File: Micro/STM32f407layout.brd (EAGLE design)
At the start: 100 x 80 mm, 41 parts, among them Q1 ASF, U1 LM1085IS-3.3

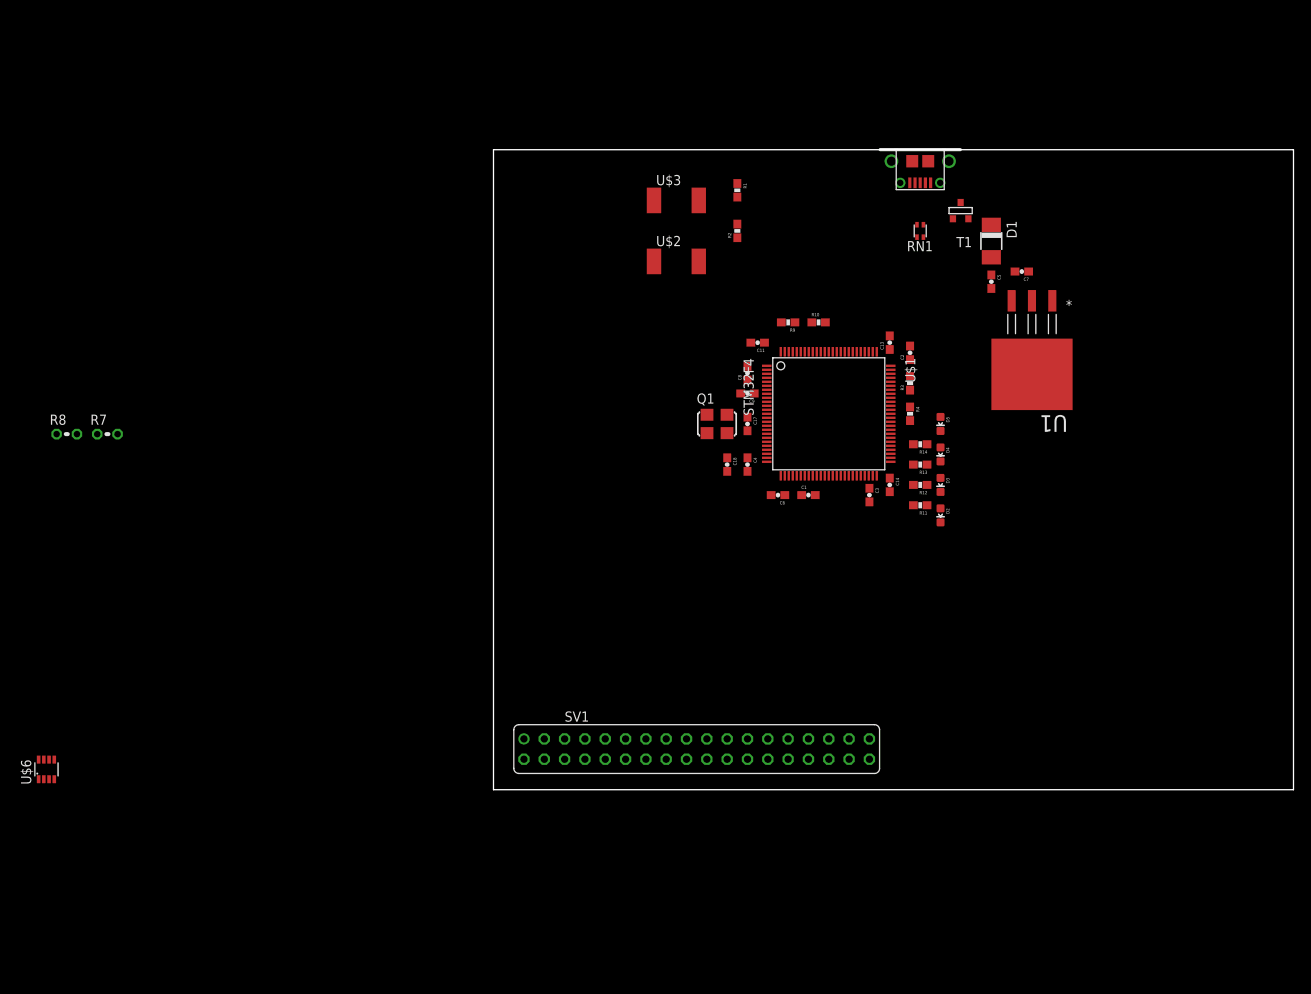
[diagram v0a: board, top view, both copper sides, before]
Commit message: worked on board layout, set initial width requirements
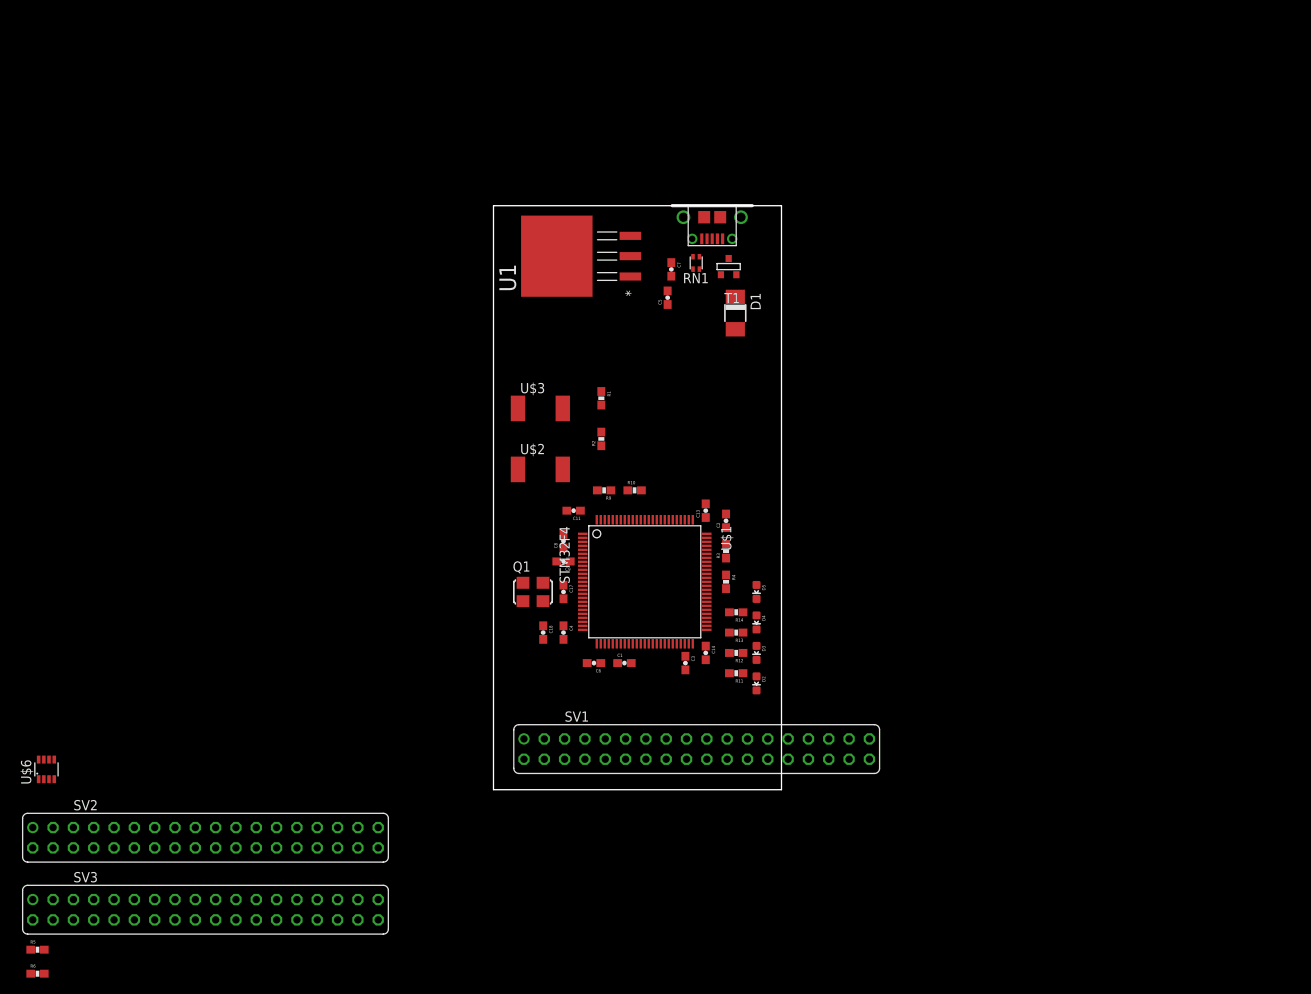
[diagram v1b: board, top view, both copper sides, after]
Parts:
- removed R7: 120, resistor:0204V
- removed R8: 100k, resistor:0204V
- added R5: 120, SparkFun-Passives:0603-RES
- added R6: 100K, SparkFun-Passives:0603-RES
- added SV2, SV3: (no value), Connectors:FE18-2
- moved U1 61.0 mm to (8.07, 66.7), turned to 90 degrees
- moved C7 43.8 mm to (22.2, 65.0), turned to 270 degrees
- moved C5 40.5 mm to (21.8, 61.5), turned to 90 degrees
- moved D1 33.2 mm to (30.2, 59.6)
- moved C11 31.1 mm to (10.0, 34.9)
- moved C3 31.1 mm to (24.0, 15.8)
- moved R11 31.1 mm to (30.3, 14.6)
- moved R12 31.1 mm to (30.3, 17.1)
- moved R13 31.1 mm to (30.3, 19.6)
- moved R14 31.1 mm to (30.3, 22.2)
- moved R4 31.1 mm to (29.1, 26.0)
- moved C1 31.1 mm to (16.4, 15.8)
- moved C13 31.1 mm to (26.5, 34.9)
- moved C14 31.1 mm to (26.5, 17.1)
- moved C17 31.1 mm to (8.75, 24.7)
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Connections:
- removed net N$13: R8.1, U$6.8
- new net N$11: R6.2, U$6.8
- net CANH1: now also R5.2; no longer R7.1
- net CANL1: now also R5.1; no longer R7.2
- net GND: now also R6.1; no longer R8.2
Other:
- board size 100 x 80 mm -> 36 x 73 mm

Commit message: Updated Board
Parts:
- removed SV1, SV2, SV3: (no value), Connectors:FE18-2
- added R7: 4.7K, SparkFun-Passives:0603-RES
- moved R6 94.5 mm to (30.0, 14.0), turned to 270 degrees
- moved R5 92.0 mm to (30.0, 10.0), turned to 90 degrees
- moved U$6 82.7 mm to (26.5, 9.88), turned to 270 degrees
- moved U$4 69.3 mm to (-0.01, 9.34), turned to 270 degrees
- moved RN1 59.4 mm to (7.15, 9.34), turned to 270 degrees
- moved T1 57.3 mm to (7.61, 12.4), turned to 270 degrees
- moved D1 50.3 mm to (5.58, 15.8), turned to 180 degrees
- moved D2 34.2 mm to (15.7, 42.9), turned to 270 degrees
- moved D5 33.9 mm to (4.28, 42.9), turned to 270 degrees
- moved D3 33.2 mm to (11.9, 42.9), turned to 270 degrees
- moved D4 33.1 mm to (8.09, 42.9), turned to 270 degrees
- moved R11 30.3 mm to (14.4, 40.3), turned to 270 degrees
- moved R14 29.7 mm to (6.82, 40.3), turned to 270 degrees
- moved R12 29.7 mm to (11.9, 40.3), turned to 270 degrees
- moved R13 29.5 mm to (9.36, 40.3), turned to 270 degrees
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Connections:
- removed net CAN1_RX: SV1.1
- removed net CAN1_TX: SV1.3
- new net TEMP_SENSE_INFO: R7.1, U$1.P81
- net +3V3: now also R7.2; no longer SV1.4
- net +5V: no longer SV1.2
- net CAN2_RX: no longer SV1.5
- net CAN2_TX: no longer SV1.7
- net GND: no longer SV1.12, SV1.6, SV1.8
- net I2C1_SCL: no longer SV1.33
- net I2C1_SDA: no longer SV1.35
- net I2C3_SCL: no longer SV1.17
- net I2C3_SDA: no longer SV1.19
- net OSC_IN: no longer SV1.15
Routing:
- net +3V3: track 0.00 -> 84.9 mm, vias 0 -> 5
- net N$9: track 0.00 -> 33.4 mm
- net N$16: track 0.00 -> 32.0 mm
- net N$8: track 0.00 -> 30.6 mm
- net N$19: track 0.00 -> 28.7 mm
- net N$22: track 0.00 -> 6.27 mm, vias 0 -> 1
- net N$15: track 0.00 -> 4.12 mm
- net OSC_IN: track 0.00 -> 3.49 mm
- net N$11: track 0.00 -> 3.46 mm
- net N$10: track 0.00 -> 3.18 mm
- net N$17: track 0.00 -> 2.85 mm
- net N$5: track 0.00 -> 2.83 mm
- net CANH1: track 0.00 -> 2.50 mm
- net CANL1: track 0.00 -> 2.40 mm
- net N$6: track 0.00 -> 2.40 mm
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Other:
- board size 36 x 73 mm -> 36 x 76 mm

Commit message: More Board Updates
Remind myself to switch LED pins
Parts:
- removed R7: 4.7K, SparkFun-Passives:0603-RES
- moved U$3 52.2 mm to (29.9, 8.66)
- moved R1 45.9 mm to (32.9, 13.5), flipped to the bottom, turned to 0 degrees
- moved R9 27.7 mm to (29.6, 22.8), turned to 45 degrees
- moved R10 23.6 mm to (27.6, 16.0), turned to 225 degrees
- moved U$2 20.0 mm to (28.1, 41.0), turned to 180 degrees
- moved D5 18.9 mm to (1.12, 24.3), turned to 0 degrees
- moved R14 16.8 mm to (3.66, 23.8), turned to 45 degrees
- moved D4 16.4 mm to (1.12, 28.1), turned to 0 degrees
- moved D2 16.3 mm to (1.12, 35.7), turned to 0 degrees
- moved R2 15.4 mm to (23.4, 36.2), turned to 135 degrees
- moved D3 15.4 mm to (1.12, 31.9), turned to 0 degrees
- moved R13 13.3 mm to (3.66, 28.4), turned to 45 degrees
- moved R4 12.6 mm to (9.93, 20.0), turned to 135 degrees
- moved R11 11.8 mm to (3.56, 35.7), turned to 45 degrees
- moved R12 11.8 mm to (3.66, 31.9), turned to 45 degrees
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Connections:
- removed net CAN2_RX: U$1.P91
- removed net CAN2_TX: U$1.P92
- removed net TEMP_SENSE_INFO: R7.1, U$1.P81
- net +3V3: no longer R7.2
- net CAN_RX: now also U$1.P91
- net CAN_TX: now also U$1.P92
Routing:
- net N$9: track 33.4 -> 0.00 mm
- net N$16: track 32.0 -> 0.00 mm
- net N$8: track 30.6 -> 0.00 mm
- net N$19: track 28.7 -> 0.00 mm
- net I2C1_SCL: track 0.00 -> 25.7 mm
- net I2C1_SDA: track 0.00 -> 23.9 mm
- net I2C3_SCL: track 0.00 -> 23.0 mm, vias 0 -> 1
- net I2C3_SDA: track 0.00 -> 21.6 mm, vias 0 -> 1
- net N$3: track 0.00 -> 19.1 mm, vias 0 -> 1
- net USB_D+: track 0.00 -> 12.1 mm
- net USB_D-: track 0.00 -> 11.5 mm
- net N$4: track 0.00 -> 10.5 mm
- net CAN_TX: track 0.00 -> 7.36 mm
- net CAN_RX: track 0.00 -> 5.52 mm
- net N$15: track 4.12 -> 0.00 mm
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
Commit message: Made changes to the micro board
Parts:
- removed C5, C7: 0.22uF, SparkFun-Passives:0603-CAP
- removed D1: (no value), DiscreteComponents:DO-214AC
- removed RN1: (no value), DiscreteComponents:EXBV4V
- removed T1: (no value), DiscreteComponents:SOT-23
- removed U$4: MICROUSB, Other:MICRO_B
- removed U1: LM1085IS-3.3, PowerComponents:TO254P1435X457-3N
- added C10, C12: 0.22uF, rcl:C0603
- added D6: (no value), DiscreteComponents:DO-214AC
- added RN2: (no value), DiscreteComponents:EXBV4V
- added SV1, SV2, SV3: (no value), con-lsta:FE08-2
- added SV4: (no value), con-lsta:FE07-2
- added T3: FDN340P, DiscreteComponents:SOT-23
- added T4: AP1117_LIN_REG, PowerComponents:SOT223
- added U$5: MICROUSB, Other:MICRO_B
- moved C1 57.5 mm to (68.0, 47.6), flipped to the top, turned to 0 degrees
- moved R4 56.7 mm to (34.6, 71.1), flipped to the bottom, turned to 0 degrees
- moved C8 53.7 mm to (55.8, 54.6), turned to 90 degrees
- moved R3 53.5 mm to (34.6, 64.9), flipped to the bottom, turned to 0 degrees
- moved R14 48.8 mm to (26.2, 67.2), turned to 0 degrees
- moved D5 48.0 mm to (22.6, 67.2), turned to 90 degrees
- moved R13 46.6 mm to (26.2, 69.1), turned to 0 degrees
- moved D4 46.3 mm to (22.6, 69.1), turned to 90 degrees
- moved R12 45.2 mm to (26.2, 71.1), turned to 0 degrees
- moved D3 44.7 mm to (22.6, 71.1), turned to 90 degrees
- moved C11 44.2 mm to (57.3, 47.5), turned to 180 degrees
- moved R11 43.7 mm to (26.2, 73.1), turned to 0 degrees
- moved Q1 43.5 mm to (68.1, 51.2), turned to 90 degrees
- moved D2 43.1 mm to (22.6, 73.1), turned to 90 degrees
- moved U$3 43.0 mm to (24.0, 51.3), turned to 270 degrees
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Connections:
- removed net ETC_MDC: U$1.P16
- removed net ETH_CRS_DV: U$1.P32
- removed net ETH_MDIO: U$1.P25
- removed net ETH_REF_CLK: U$1.P24
- removed net ETH_RXD0: U$1.P33
- removed net ETH_RXD1: U$1.P34
- removed net ETH_TXD0: U$1.P51
- removed net ETH_TXD1: U$1.P52
- removed net ETH_TX_EN: U$1.P48
- removed net N$10: T1.1, U$4.P1
- removed net N$16: R13.2, U$1.P60
- removed net N$19: R11.2, U$1.P58
- removed net N$22: C17.2, C18.2, U$1.P20
- removed net N$5: D1.C, T1.2
- removed net N$6: RN1.2, U$4.P3
- removed net N$7: RN1.1, U$4.P2
- removed net N$8: R12.2, U$1.P59
- removed net N$9: R14.2, U$1.P61
- removed net VCC: U$6.3
- new net CRS_DV: SV4.7, U$1.P32
- new net MDC: SV4.5, U$1.P16
- new net MDIO: SV4.6, U$1.P25
- new net N$12: RN2.1, U$5.P2
- new net N$24: RN2.2, U$5.P3
- new net N$57: T3.1, U$5.P1
- new net N$58: C12.1, D6.C, T3.2, T4.VIN
- new net PA10: SV2.14, U$1.P69
- new net PA13: U$1.P72
- new net PA14: U$1.P76
- new net PA15: U$1.P77
- new net PA5: U$1.P31
- new net PA9: SV2.13, U$1.P68
- new net PB0: U$1.P35
- new net PB1: U$1.P36
- new net PB10: U$1.P47
- new net PB14: U$1.P53
- new net PB15: U$1.P54
- new net PB2: U$1.P37
- new net PB3: U$1.P89
- new net PB4: SV1.11, U$1.P90
- new net PB9: SV1.16, U$1.P96
- new net PC0: SV3.1, U$1.P15
- new net PC10: SV1.1, U$1.P78
- new net PC11: SV1.2, U$1.P79
- new net PC12: SV1.3, U$1.P80
- new net PC13: SV3.6, U$1.P7
- new net PC14: SV3.5, U$1.P8
- new net PC15: SV3.4, U$1.P9
- new net PC2: U$1.P17
- new net PC3: U$1.P18
- new net PC6: SV2.8, U$1.P63
- new net PC7: SV2.9, U$1.P64
- new net PC8: SV2.10, U$1.P65
- new net PD0: SV1.4, U$1.P81
- new net PD1: SV1.5, U$1.P82
- new net PD10: U$1.P57
- new net PD11: R11.2, SV2.3, U$1.P58
- new net PD12: R12.2, SV2.4, U$1.P59
- new net PD13: R13.2, SV2.5, U$1.P60
- new net PD14: R14.2, SV2.6, U$1.P61
- new net PD15: SV2.7, U$1.P62
- new net PD2: SV1.6, U$1.P83
- new net PD3: SV1.7, U$1.P84
- new net PD4: SV1.8, U$1.P85
- new net PD5: SV1.9, U$1.P86
- new net PD6: SV1.10, U$1.P87
- new net PD7: U$1.P88
- new net PD8: SV2.1, U$1.P55
- new net PD9: SV2.2, U$1.P56
- new net PE0: U$1.P97
- new net PE1: U$1.P98
- new net PE10: U$1.P41
- new net PE11: U$1.P42
- new net PE12: U$1.P43
- new net PE13: U$1.P44
- new net PE14: U$1.P45
- new net PE15: U$1.P46
- new net PE2: SV3.16, U$1.P1
- new net PE3: SV3.15, U$1.P2
- new net PE4: SV3.14, U$1.P3
- new net PE5: SV3.13, U$1.P4
- new net PE6: SV3.12, U$1.P5
- new net PE7: U$1.P38
- new net PE8: U$1.P39
- new net PE9: U$1.P40
- new net PH1: SV3.2, U$1.P13
- new net REFCLK: SV4.8, U$1.P24
- new net RXD0: SV4.10, U$1.P33
- new net RXD1: SV4.9, U$1.P34
- new net TXD0: SV4.11, U$1.P51
- new net TXD1: SV4.14, U$1.P52
- new net TXEN: SV4.12, U$1.P48
- net +3V3: now also C10.1, SV2.16, SV3.10, SV3.8, SV4.1, SV4.2, T4.TAB, T4.VOUT, U$6.3; no longer C7.1, U1.2, U1.4
- net +5V: now also D6.A, T3.3; no longer C5.1, D1.A, T1.3, U1.3
- net CAN_RX: now also SV1.12
- net CAN_TX: now also SV1.13
- net GND: now also C10.2, C12.2, C17.2, C18.2, SV2.15, SV3.11, SV3.7, SV3.9, SV4.3, SV4.4, T4.GND, U$1.P20, U$5.GND1, U$5.GND2, U$5.GND3, U$5.GND4, U$5.GND7, U$5.GND8, U$5.P4, U$5.P5; no longer C5.2, C7.2, U$4.GND1, U$4.GND2, U$4.GND3, U$4.GND4, U$4.GND7, U$4.GND8, U$4.P4, U$4.P5, U1.1
- net I2C1_SCL: now also SV1.15
- net I2C1_SDA: now also SV1.14
- net I2C3_SCL: now also SV2.12
- net I2C3_SDA: now also SV2.11
- net OSC_IN: now also SV3.3
- net USB_D+: now also RN2.3; no longer RN1.3
- net USB_D-: now also RN2.4; no longer RN1.4
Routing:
- net +3V3: track 85.9 -> 145.8 mm, vias 8 -> 7
- net N$4: track 10.5 -> 47.6 mm, vias 0 -> 3
- net PD11: track 0.00 -> 35.0 mm, vias 0 -> 1
- net PD12: track 0.00 -> 33.9 mm, vias 0 -> 1
- net PD13: track 0.00 -> 32.5 mm, vias 0 -> 1
- net PD14: track 0.00 -> 31.0 mm, vias 0 -> 1
- net N$3: track 19.1 -> 35.6 mm, vias 1 -> 2
- net I2C3_SDA: track 21.6 -> 5.44 mm, vias 1 -> 0
- net PC0: track 0.00 -> 15.8 mm
- net GND: track 0.00 -> 15.3 mm, vias 0 -> 1
- net I2C1_SCL: track 25.7 -> 10.6 mm
- net N$57: track 0.00 -> 15.0 mm
- net OSC_IN: track 3.68 -> 18.4 mm
- net PC14: track 0.00 -> 14.4 mm
- net I2C3_SCL: track 23.0 -> 9.46 mm, vias 1 -> 0
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- added copper zone on layer 1, net +3V3
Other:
- board size 36 x 76 mm -> 100 x 80 mm

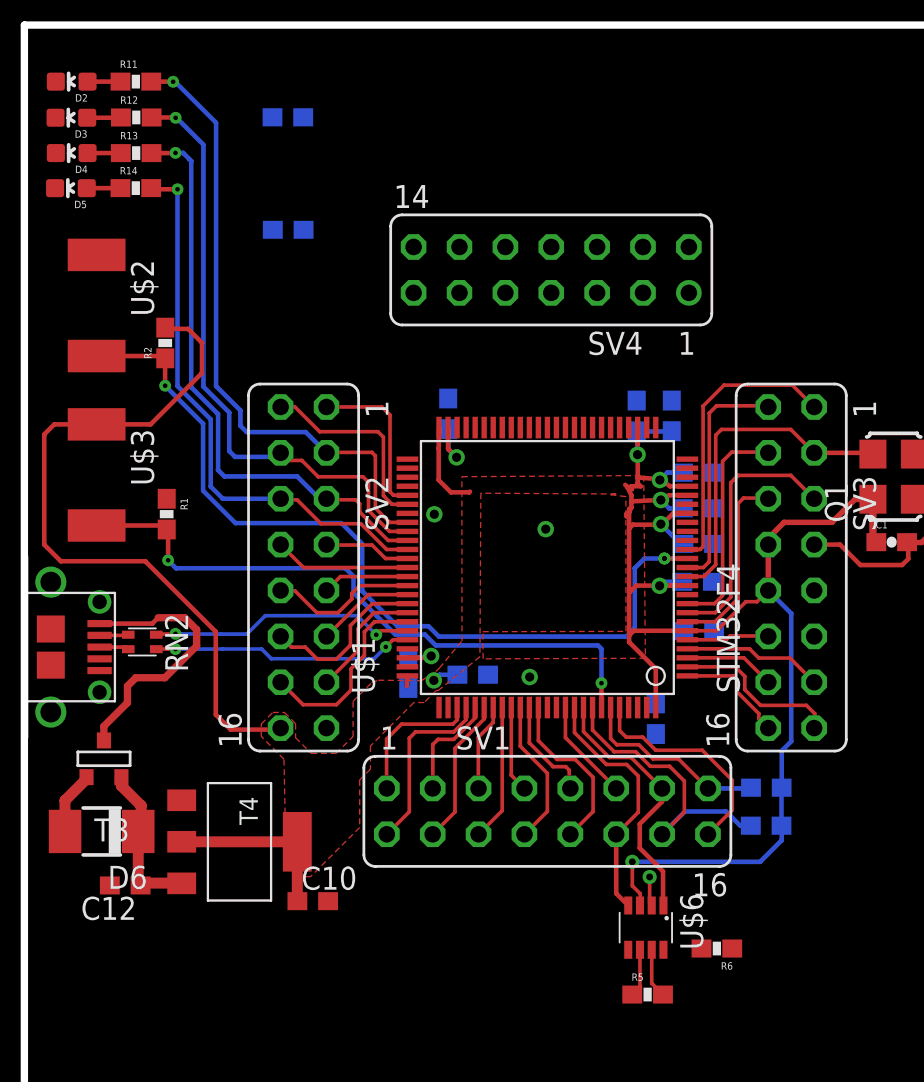
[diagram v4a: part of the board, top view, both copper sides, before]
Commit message: Updated Board on flight
moved TXD0 pin connection to not cross transmission lines
remove PC0 so can run MDC out. If it is a clock its pretty important
that it does not go under micro
may want to move xtal, bit far away probably wont be a problem but hf
signals do not like distance and things inbetween them
check via usage, use different ones , may want to stick to 1 size
move i2c resistors to bottom, connected them to 3v3
are linear regs noisey or is that switching? pretty sure it is switching
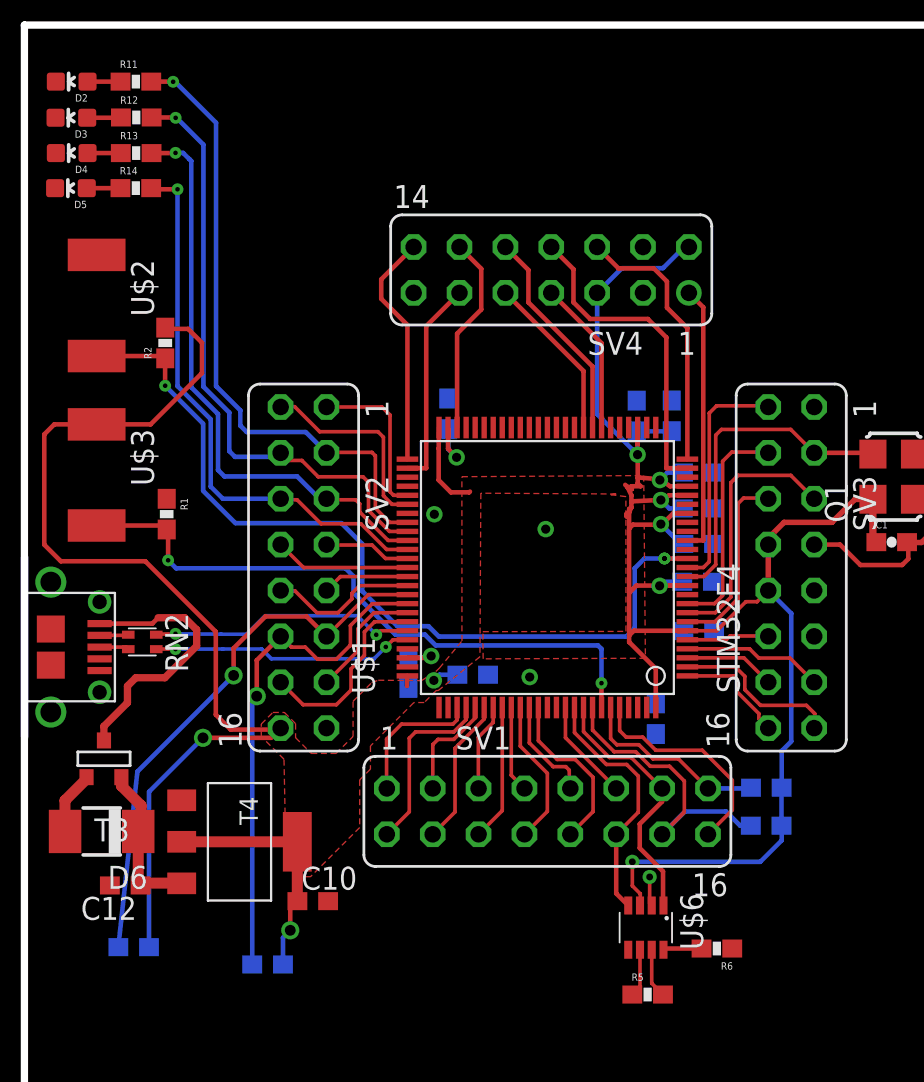
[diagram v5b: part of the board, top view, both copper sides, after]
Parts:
- moved R4 46.7 mm to (26.0, 25.1), turned to 180 degrees
- moved R3 40.7 mm to (33.5, 24.2), turned to 180 degrees
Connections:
- net +3V3: now also SV4.5; no longer SV4.1
- net MDC: now also SV4.1; no longer SV4.5
- net TXD0: now also SV4.14; no longer SV4.11
- net TXD1: now also SV4.11; no longer SV4.14
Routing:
- net +3V3: track 145.8 -> 184.5 mm, vias 7 -> 9
- net I2C3_SDA: track 5.44 -> 30.6 mm, vias 0 -> 1
- net I2C3_SCL: track 9.46 -> 28.3 mm, vias 0 -> 1
- net REFCLK: track 0.00 -> 17.9 mm
- net PC0: track 15.8 -> 0.00 mm
- net MDIO: track 0.00 -> 15.0 mm
- net MDC: track 0.00 -> 14.9 mm
- net TXD0: track 0.00 -> 13.1 mm
- net RXD0: track 0.00 -> 12.0 mm
- net TXD1: track 0.00 -> 11.5 mm
- net TXEN: track 0.00 -> 11.1 mm
- net RXD1: track 0.00 -> 9.25 mm
- net CRS_DV: track 0.00 -> 8.61 mm
- net N$11: track 0.00 -> 2.14 mm
